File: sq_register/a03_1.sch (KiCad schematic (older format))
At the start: 26 parts, among them U3001 74HC02, U3002 74HC27, U3003 74HC04, U3004 74HC02, U3005 74HC02, U3006 74HC27, U3007 74HC02, U3008 74HC04, U3009 74HC27, U3010 74HC27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

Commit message: Added the final four bit module. All 16 bits of the central/special registers are present. We're stuck at address 0 because TC is using RAD, which needs to be translated into RG or RZ by module 12
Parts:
- U3003: Initial (none) -> 1
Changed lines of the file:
@@
 F 2 "" H 5450 2600 60  0000 C CNN
 F 3 "" H 5450 2600 60  0000 C CNN
+F 4 "1" H 5500 2600 60  0000 C CIN "Initial"
 	2    5450 2600
 	1    0    0    -1
@@
 F 2 "" H 8250 3150 60  0000 C CNN
 F 3 "" H 8250 3150 60  0000 C CNN
+F 4 "1" H 8300 3150 60  0000 C CIN "Initial"
 	3    8250 3150
 	1    0    0    -1

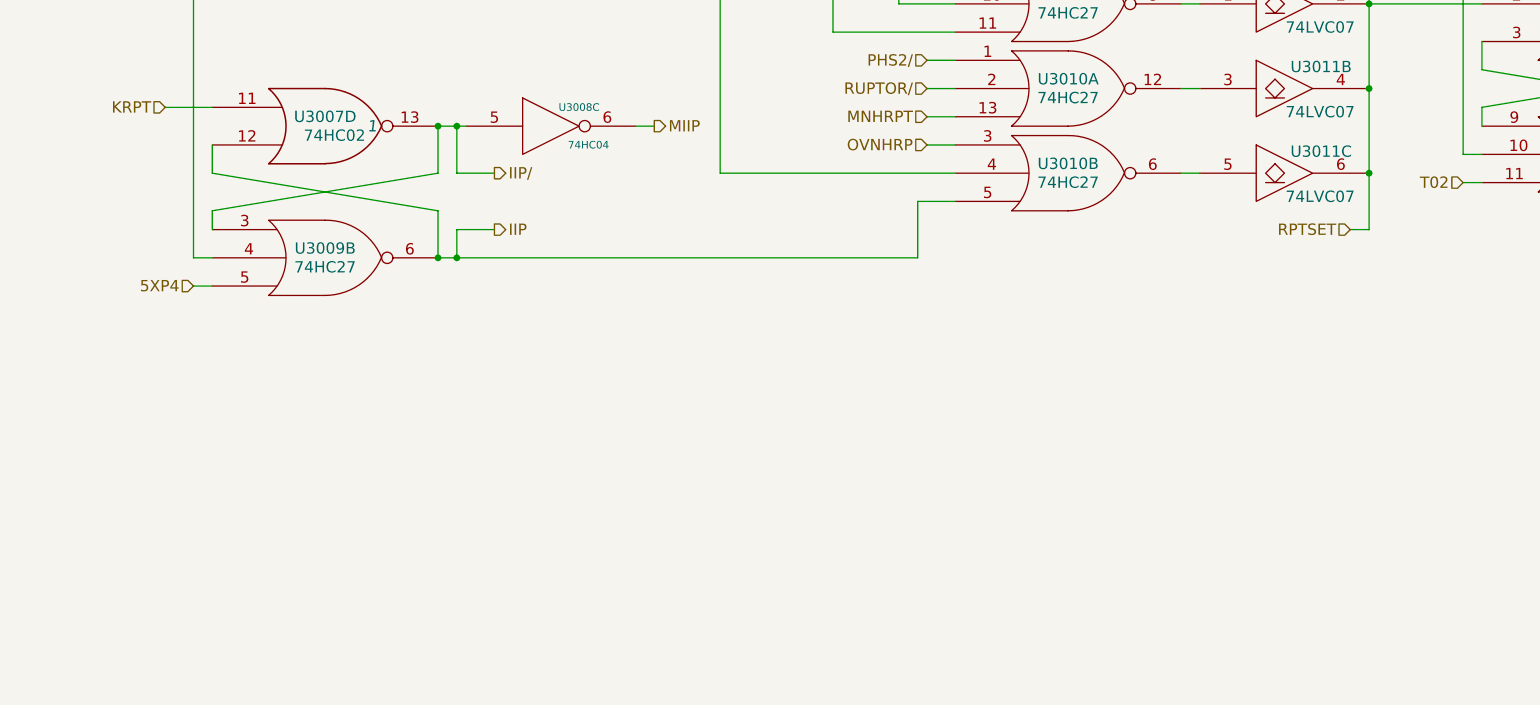
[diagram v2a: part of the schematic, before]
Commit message: Added interrupt inhibition to module 3
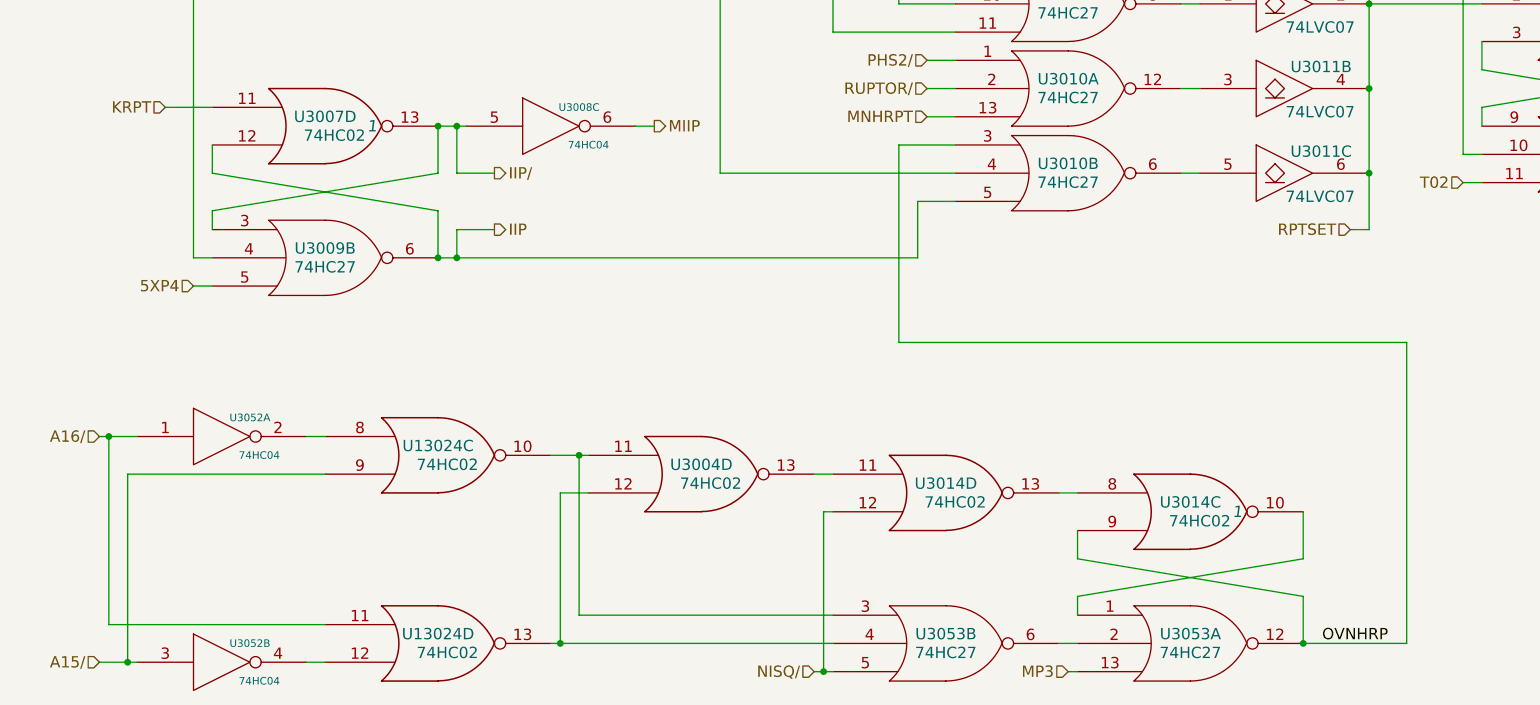
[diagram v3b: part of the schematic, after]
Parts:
- added U13024: 74HC02, symbol 74HC02
- added unit 4 of U3004
- added unit 3 of U3014
- added unit 4 of U3014
- added U3052: 74HC04, symbol 74HC04
- added U3053: 74HC27, symbol 74HC27
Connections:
- net GND: now also U13024.7 (GND), U13024.7 (GND), U3004.7 (GND), U3014.7 (GND), U3014.7 (GND), U3052.7 (GND), U3052.7 (GND), U3053.7 (GND), U3053.7 (GND)
- net OVNHRP: now also U3014.9, U3053.12
- net VCC: now also U13024.14 (VCC), U13024.14 (VCC), U3004.14 (VCC), U3014.14 (VCC), U3014.14 (VCC), U3052.14 (VCC), U3052.14 (VCC), U3053.14 (VCC), U3053.14 (VCC)
- new net: U13024.8, U3052.2
- new net: U13024.12, U3052.4
- new net: U3014.10, U3053.1
- new net: U3014.13, U3014.8
- new net: U3053.2, U3053.6
- new net: U13024.10, U3004.11, U3053.3
- new net: U13024.13, U3004.12, U3053.4
- new net: U3004.13, U3014.11
- new net A15/: U13024.9, U3052.3
- new net A16/: U13024.11, U3052.1
- new net MP3: U3053.13
- new net NISQ/: U3014.12, U3053.5
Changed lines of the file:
@@
 Text HLabel 5750 9000 0    60   Input ~ 0
 MNHRPT
-Text HLabel 5750 9150 0    60   Input ~ 0
-OVNHRP
 $Comp
 L R R3001
@@
 	5750 9000 5900 9000
 Wire Wire Line
-	5750 9150 5900 9150
+	5600 9150 5900 9150
 Wire Wire Line
 	5700 9750 5700 9450
@@
 Wire Wire Line
 	900  1450 900  3300
+$Comp
+L 74HC04 U3052
+U 1 1 57173C92
+P 2000 10700
+F 0 "U3052" H 2150 10800 40  0000 C CNN
+F 1 "74HC04" H 2200 10600 40  0000 C CNN
+F 2 "" H 2000 10700 60  0000 C CNN
+F 3 "" H 2000 10700 60  0000 C CNN
+	1    2000 10700
+	1    0    0    -1
+$EndComp
+$Comp
+L 74HC04 U3052
+U 2 1 57174ECD
+P 2000 11900
+F 0 "U3052" H 2150 12000 40  0000 C CNN
+F 1 "74HC04" H 2200 11800 40  0000 C CNN
+F 2 "" H 2000 11900 60  0000 C CNN
+F 3 "" H 2000 11900 60  0000 C CNN
+	2    2000 11900
+	1    0    0    -1
+$EndComp
+$Comp
+L 74HC02 U3014
+U 3 1 5717523D
+P 7150 11100
+F 0 "U3014" H 7150 11150 60  0000 C CNN
+F 1 "74HC02" H 7200 11050 60  0000 C CNN
+F 2 "" H 7150 11100 60  0000 C CNN
+F 3 "" H 7150 11100 60  0000 C CNN
+F 4 "1" H 7400 11100 60  0000 C CIN "Initial"
+	3    7150 11100
+	1    0    0    -1
+$EndComp
+$Comp
+L 74HC27 U3053
+U 1 1 57175573
+P 7150 11800
+F 0 "U3053" H 7150 11850 60  0000 C CNN
+F 1 "74HC27" H 7150 11750 60  0000 C CNN
+F 2 "" H 7150 11800 60  0000 C CNN
+F 3 "" H 7150 11800 60  0000 C CNN
+	1    7150 11800
+	1    0    0    -1
+$EndComp
+Wire Wire Line
+	7750 11800 7750 11550
+Wire Wire Line
+	7750 11550 6550 11350
+Wire Wire Line
+	6550 11350 6550 11200
+Wire Wire Line
+	7750 11100 7750 11350
+Wire Wire Line
+	7750 11350 6550 11550
+Wire Wire Line
+	6550 11550 6550 11650
+$Comp
+L 74HC27 U3053
+U 2 1 57175F88
+P 5850 11800
+F 0 "U3053" H 5850 11850 60  0000 C CNN
+F 1 "74HC27" H 5850 11750 60  0000 C CNN
+F 2 "" H 5850 11800 60  0000 C CNN
+F 3 "" H 5850 11800 60  0000 C CNN
+	2    5850 11800
+	1    0    0    -1
+$EndComp
+Wire Wire Line
+	6450 11800 6550 11800
+Wire Wire Line
+	6550 11950 6500 11950
+Text HLabel 6500 11950 0    60   Input ~ 0
+MP3
+$Comp
+L 74HC02 U3014
+U 4 1 571769B1
+P 5850 11000
+F 0 "U3014" H 5850 11050 60  0000 C CNN
+F 1 "74HC02" H 5900 10950 60  0000 C CNN
+F 2 "" H 5850 11000 60  0000 C CNN
+F 3 "" H 5850 11000 60  0000 C CNN
+	4    5850 11000
+	1    0    0    -1
+$EndComp
+Wire Wire Line
+	6450 11000 6550 11000
+$Comp
+L 74HC02 U3004
+U 4 1 571799C2
+P 4550 10900
+F 0 "U3004" H 4550 10950 60  0000 C CNN
+F 1 "74HC02" H 4600 10850 60  0000 C CNN
+F 2 "" H 4550 10900 60  0000 C CNN
+F 3 "" H 4550 10900 60  0000 C CNN
+	4    4550 10900
+	1    0    0    -1
+$EndComp
+Wire Wire Line
+	5150 10900 5250 10900
+$Comp
+L 74HC02 U13024
+U 3 1 57179E90
+P 3150 10800
+F 0 "U13024" H 3150 10850 60  0000 C CNN
+F 1 "74HC02" H 3200 10750 60  0000 C CNN
+F 2 "" H 3150 10800 60  0000 C CNN
+F 3 "" H 3150 10800 60  0000 C CNN
+	3    3150 10800
+	1    0    0    -1
+$EndComp
+$Comp
+L 74HC02 U13024
+U 4 1 5717A156
+P 3150 11800
+F 0 "U13024" H 3150 11850 60  0000 C CNN
+F 1 "74HC02" H 3200 11750 60  0000 C CNN
+F 2 "" H 3150 11800 60  0000 C CNN
+F 3 "" H 3150 11800 60  0000 C CNN
+	4    3150 11800
+	1    0    0    -1
+$EndComp
+Wire Wire Line
+	3750 11800 5250 11800
+Wire Wire Line
+	2450 11900 2550 11900
+Wire Wire Line
+	2450 10700 2550 10700
+Wire Wire Line
+	3750 10800 3950 10800
+Wire Wire Line
+	5250 11100 5200 11100
+Wire Wire Line
+	5200 11100 5200 11950
+Wire Wire Line
+	5150 11950 5250 11950
+Connection ~ 5200 11950
+Text HLabel 5150 11950 0    60   Input ~ 0
+NISQ/
+Wire Wire Line
+	3800 11800 3800 11000
+Wire Wire Line
+	3800 11000 3950 11000
+Connection ~ 3800 11800
+Wire Wire Line
+	3900 10800 3900 11650
+Wire Wire Line
+	3900 11650 5250 11650
+Connection ~ 3900 10800
+Wire Wire Line
+	1350 10700 1550 10700
+Text HLabel 1350 10700 0    60   Input ~ 0
+A16/
+Wire Wire Line
+	1350 11900 1550 11900
+Text HLabel 1350 11900 0    60   Input ~ 0
+A15/
+Wire Wire Line
+	1500 11900 1500 10900
+Wire Wire Line
+	1500 10900 2550 10900
+Connection ~ 1500 11900
+Wire Wire Line
+	1400 10700 1400 11700
+Wire Wire Line
+	1400 11700 2550 11700
+Connection ~ 1400 10700
+Connection ~ 7750 11800
+Wire Wire Line
+	7750 11800 8300 11800
+Text Label 7850 11800 0    60   ~ 0
+OVNHRP
+Wire Wire Line
+	8300 11800 8300 10200
+Wire Wire Line
+	8300 10200 5600 10200
+Wire Wire Line
+	5600 10200 5600 9150
 $EndSCHEMATC

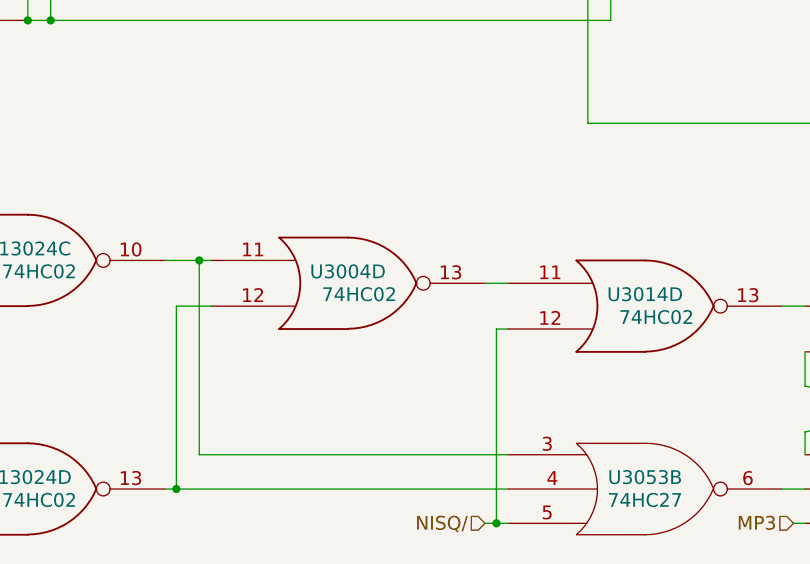
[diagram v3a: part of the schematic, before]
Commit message: Lots of initial conditions, some missed gates, and some wiring fixes
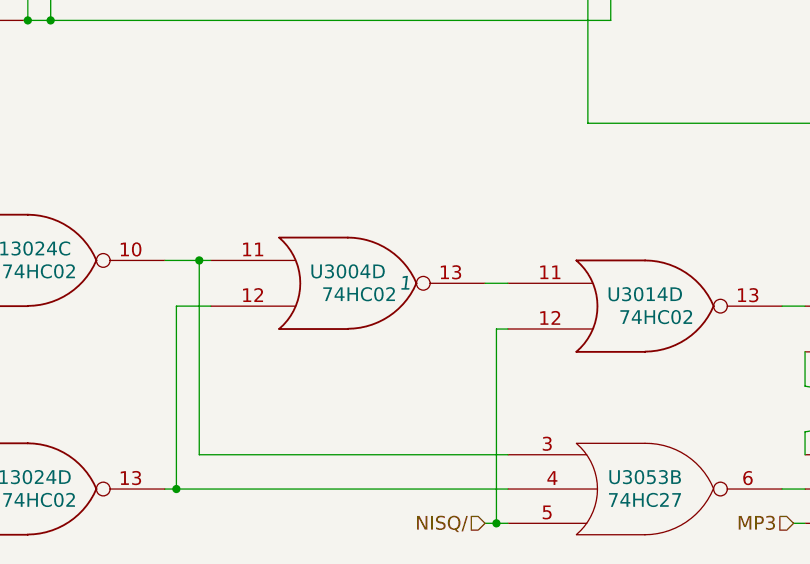
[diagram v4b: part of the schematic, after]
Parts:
- U3004: Initial (none) -> 1
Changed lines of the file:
@@
 F 2 "" H 4550 10900 60  0000 C CNN
 F 3 "" H 4550 10900 60  0000 C CNN
+F 4 "1" H 4800 10900 60  0000 C CIN "Initial"
 	4    4550 10900
 	1    0    0    -1

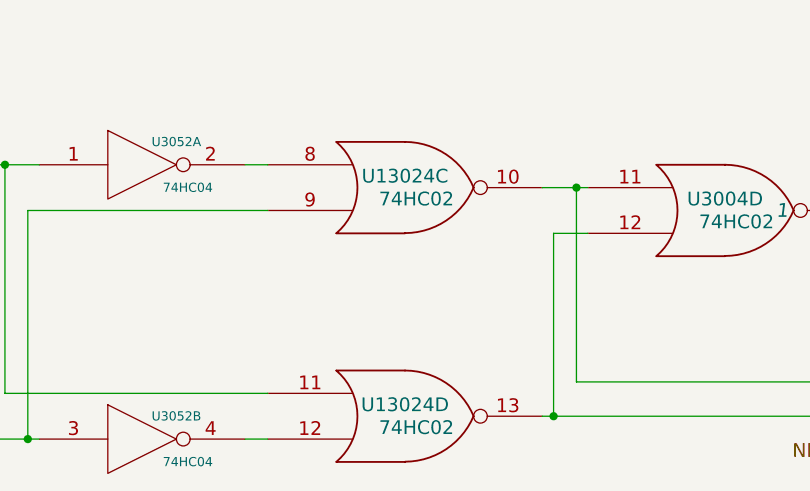
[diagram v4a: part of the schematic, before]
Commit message: Corrected some bad part identifiers
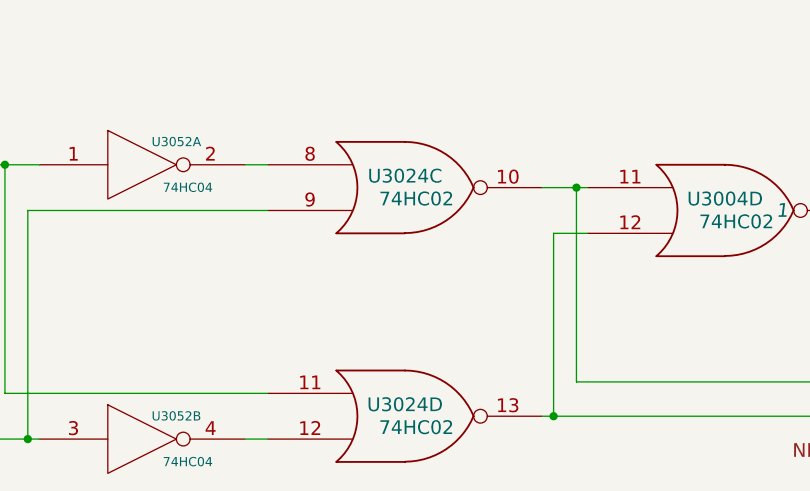
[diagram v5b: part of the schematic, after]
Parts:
- renumbered U13024 to U3024
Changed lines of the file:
@@
 	5150 10900 5250 10900
 $Comp
-L 74HC02 U13024
+L 74HC02 U3024
 U 3 1 57179E90
 P 3150 10800
-F 0 "U13024" H 3150 10850 60  0000 C CNN
+F 0 "U3024" H 3150 10850 60  0000 C CNN
 F 1 "74HC02" H 3200 10750 60  0000 C CNN
 F 2 "" H 3150 10800 60  0000 C CNN
@@
 $EndComp
 $Comp
-L 74HC02 U13024
+L 74HC02 U3024
 U 4 1 5717A156
 P 3150 11800
-F 0 "U13024" H 3150 11850 60  0000 C CNN
+F 0 "U3024" H 3150 11850 60  0000 C CNN
 F 1 "74HC02" H 3200 11750 60  0000 C CNN
 F 2 "" H 3150 11800 60  0000 C CNN

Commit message: Not gate rewiring up through module 11, with other cleanup here and there
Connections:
- wire segments 369 -> 382
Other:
- moved on the sheet: U3001A, U3002A, U3003A, U3003B, U3003C, U3003E, U3003F, U3008A, U3008B, U3008C, U3008D, U3008E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

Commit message: Switched SQ Register & Decoder over to +4VSW and fixed some straggling VCCs in Timer
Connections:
- net labels added: +4VSW
- net labels removed: VCC
